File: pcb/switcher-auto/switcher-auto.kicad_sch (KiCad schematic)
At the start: 20 parts, among them J0 MD-90SM, J5 Conn_02x22_Top_Bottom, SW1 SW_Push, SW2 SW_Push, U1 CD74HC4067SM96, U2 CD74HC4067SM96, U3 CD74HC4067SM96, U4 CD74HC4067SM96, U5 CD74HC4067SM96, U6 CD74HC4067SM96, U7 CD74HC4067SM96

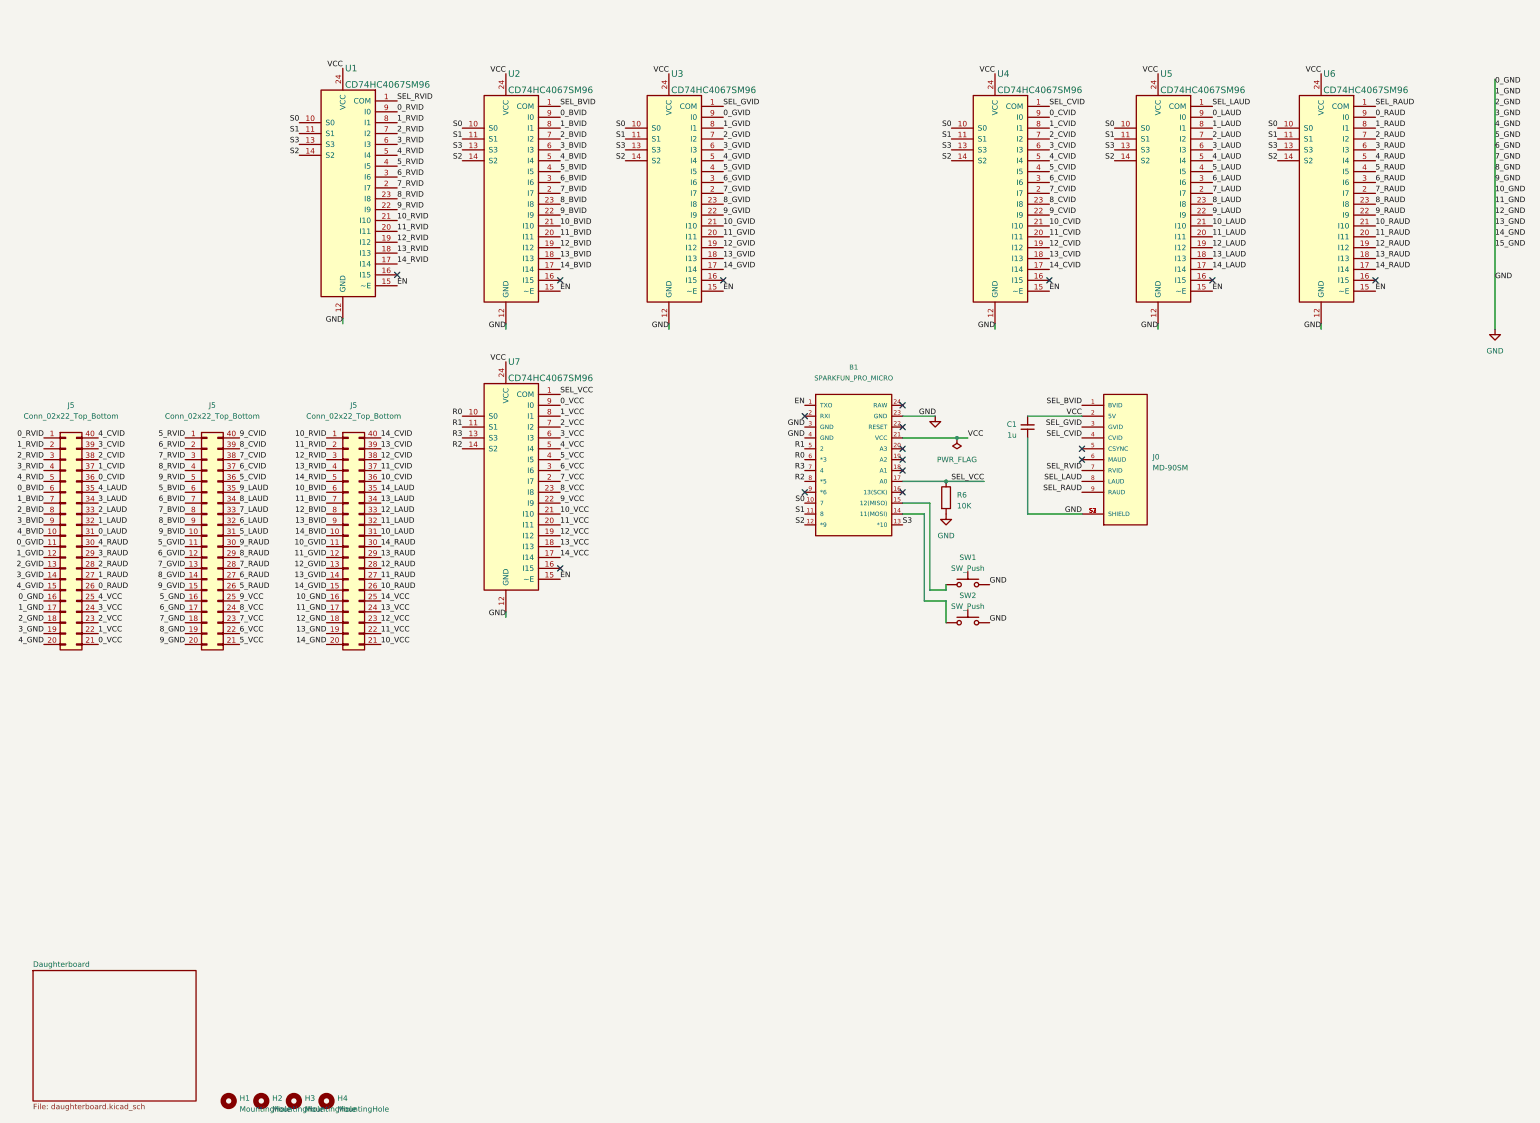
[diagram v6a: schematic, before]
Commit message: decouple every mux
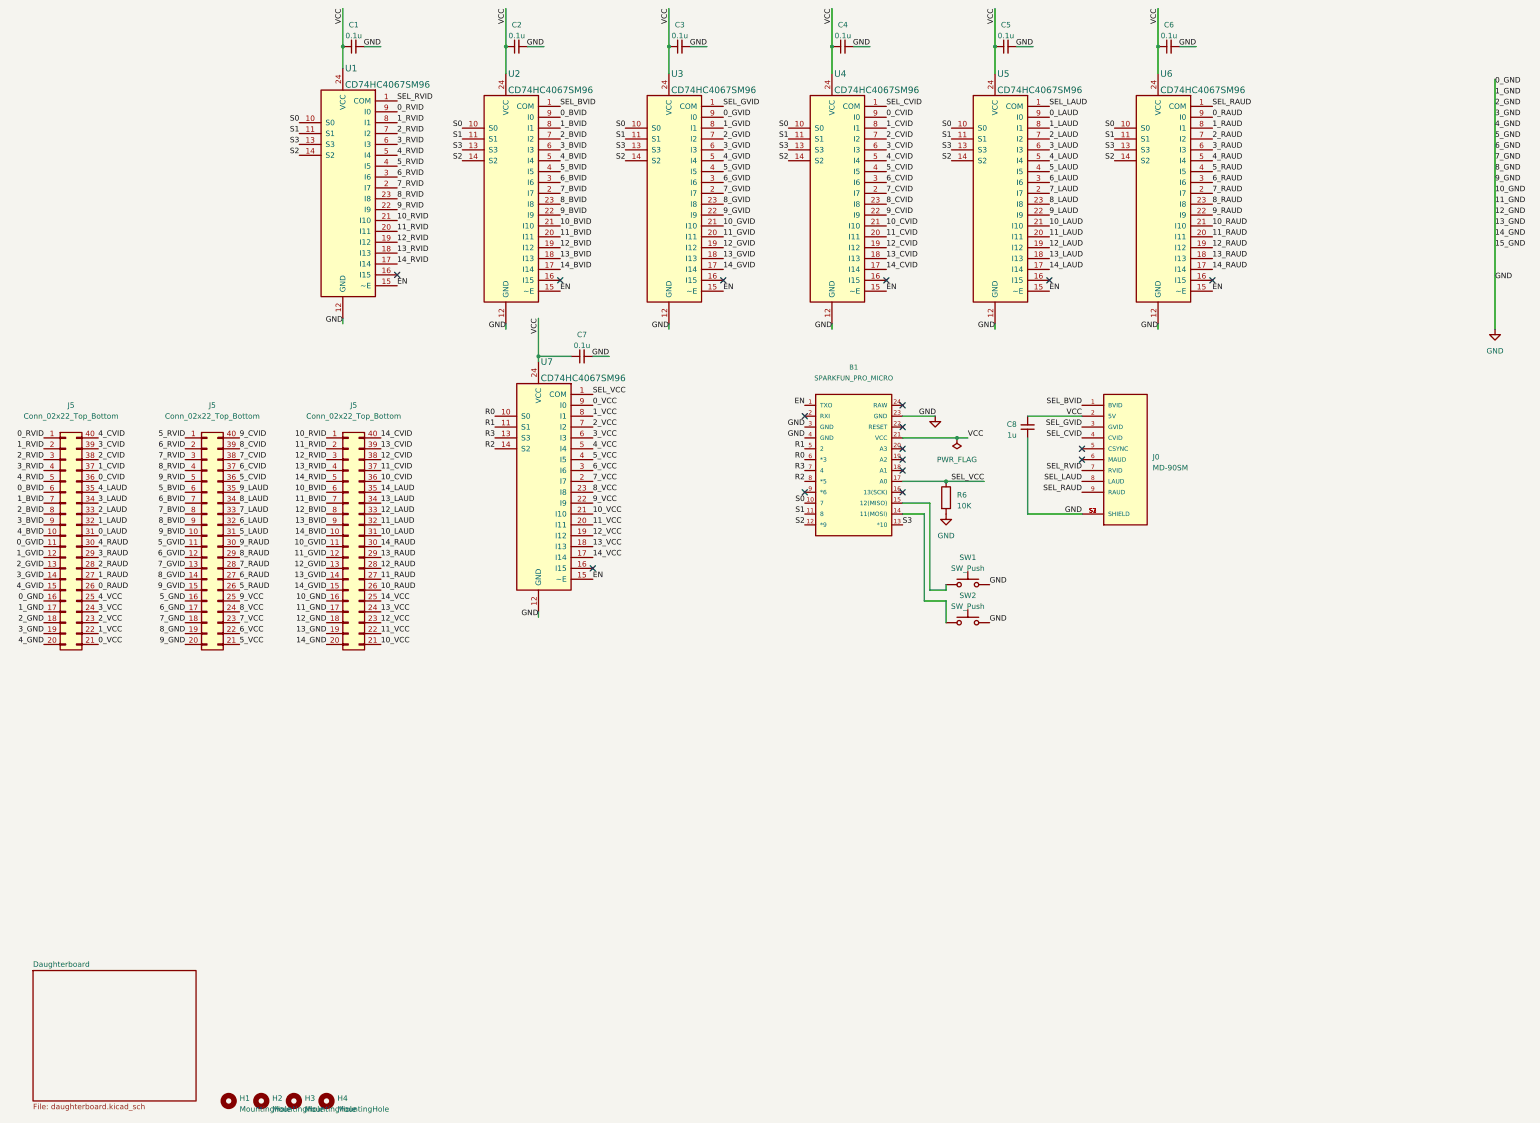
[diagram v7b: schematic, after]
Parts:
- added C1, C2, C3, C4, C5, C6, C7: 0.1u, Capacitor_SMD:C_0805_2012Metric_Pad1.18x1.45mm_HandSolder, symbol Device:C_Small
- renumbered C1 to C8
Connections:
- net GND: now also C1.2, C2.2, C3.2, C4.2, C5.2, C6.2, C7.2
- net VCC: now also C1.1, C2.1, C3.1, C4.1, C5.1, C6.1, C7.1
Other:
- moved on the sheet: U4, U5, U6, U7

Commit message: WIP
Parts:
- removed H1, H2, H3, H4: MountingHole, MountingHole:MountingHole_2.5mm, symbol Mechanical:MountingHole
- U1, U2, U3, U4, U5, U6, U7: footprint Package_SO:SSOP-24_5.3x8.2mm_P0.65mm -> Package_SO:SOIC-24W_7.5x15.4mm_P1.27mm; symbol dk_Interface-Analog-Switches-Multiplexers-Demultiplexers:CD74HC4067SM96 -> REB-DIN:CD4067BM96
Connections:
- net R0: no longer U7.10 (S0)
- net R1: no longer U7.11 (S1)
- net R2: no longer U7.14 (S2)
- net R3: no longer U7.13 (S3)
- net S0: now also U7.10 (S0)
- net S1: now also U7.11 (S1)
- net S2: now also U7.14 (S2)
- net S3: now also U7.13 (S3)
- no-connect marks 17 -> 10
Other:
- moved on the sheet: C1, C2, C3, C4, C5, C6, C7, U1, U2, U3, U4, U5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
